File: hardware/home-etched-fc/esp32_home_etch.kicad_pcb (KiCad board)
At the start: 2 copper layers, 100 x 100 mm, 41 parts, among them J1 DevKitC-1 LEFT 1x22, J10 ESC_RR, J11 ESC_RL, J12 OPTIONAL 3V3 UART, J13 F2 MINI: VCC TBD, J14 0-2.5V current input, J2 DevKitC-1 RIGHT 1x22, J3 REGULATED 5V ONLY, J4 MPU6050, J5 BMP280, J6 HMC5883L, J7 SENSE ONLY, J8 ESC_FL, J9 ESC_FR

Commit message: Retain connected ground copper and print three text-free toner masks per A4
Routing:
- added copper zone on B.Cu, net GND

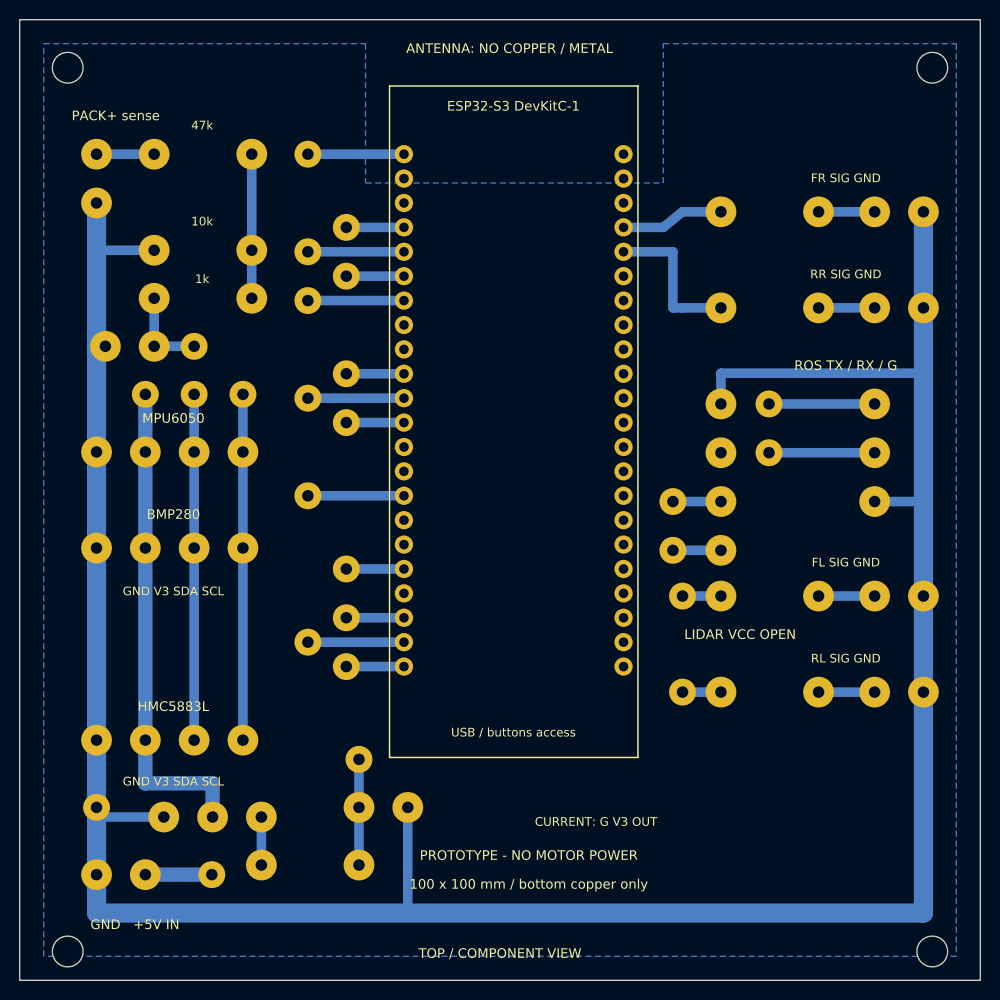
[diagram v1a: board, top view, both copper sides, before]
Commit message: Unify ESP32 firmware, verify optional ROS2 fallback and connect DevKit grounds directly
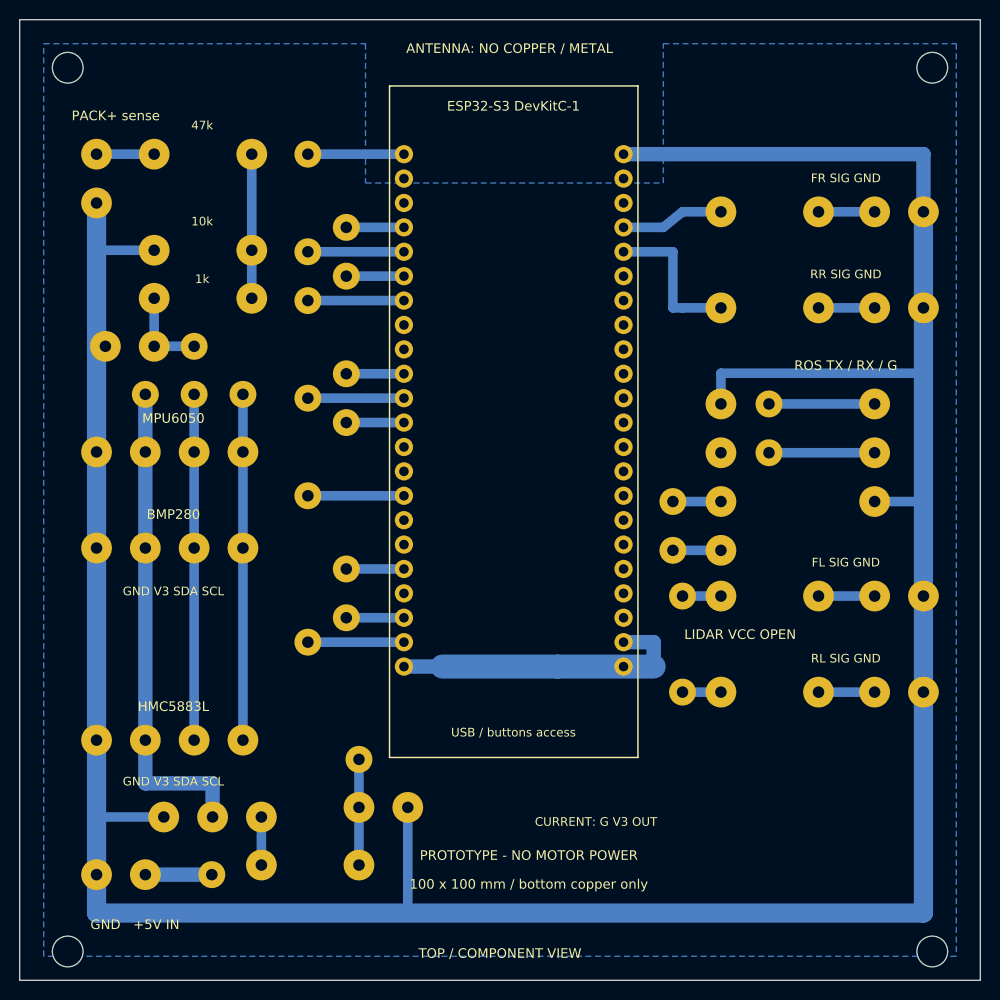
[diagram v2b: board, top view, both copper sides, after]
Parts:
- removed W22: INSULATED_WIRE, HomeEtch:W22
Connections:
- J1 pad 22: GND_MCU -> GND
- J2 pad 1: unconnected-(J2-Pad1) -> GND
- J2 pad 21: unconnected-(J2-Pad21) -> GND
- J2 pad 22: unconnected-(J2-Pad22) -> GND
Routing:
- net GND: track 287.3 -> 359.3 mm
- net GND_MCU: track 6.00 -> 0.00 mm

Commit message: Use solid common-ground pads and verify PCB power rails and toner mask
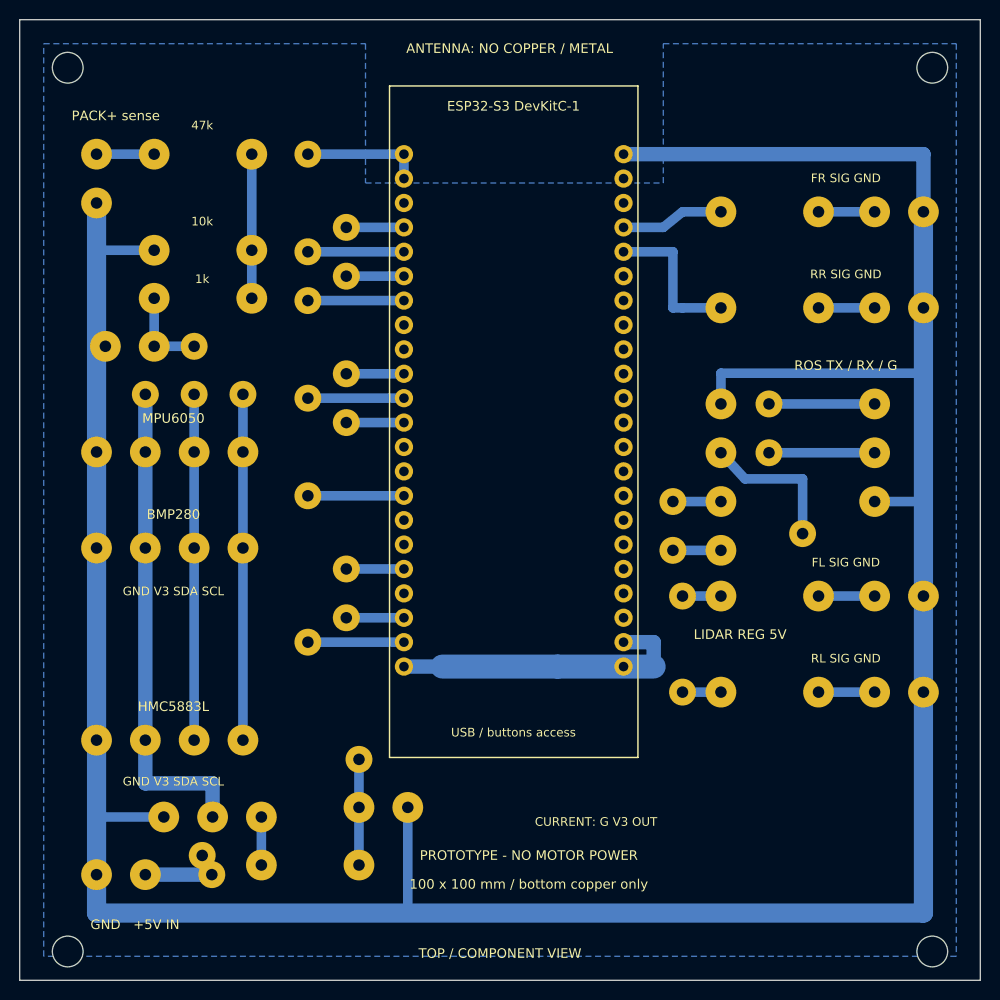
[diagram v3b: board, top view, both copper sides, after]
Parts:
- added W23: INSULATED_WIRE, HomeEtch:W23, F.Cu at (19.0, 87.0)
- J13: value F2 MINI: VCC TBD -> F2 MINI: REG 5V
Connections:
- J1 pad 2: unconnected-(J1-Pad2) -> 3V3
- J13 pad 2: unconnected-(J13-Pad2) -> LIDAR_5V
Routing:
- net LIDAR_5V: track 0.00 -> 15.4 mm
- net 3V3: track 10.0 -> 12.5 mm
- net 5V_EXT: track 6.92 -> 9.16 mm
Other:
- board text added: "LIDAR REG 5V"
- board text removed: "LIDAR VCC OPEN"

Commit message: Verify PCB reference dimensions and regenerate three actual-size copper masks
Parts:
- C1, C2: value 100nF -> 100nF X7R 5mm
- J4: value MPU6050 -> MPU6050 WIRE PORT
- J5: value BMP280 -> BMP280 WIRE PORT
- J6: value HMC5883L -> HMC5883L WIRE PORT
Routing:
- net GND: track 359.3 -> 356.4 mm

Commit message: Fix photo-matched sensor headers and verify single-sided PCB mask
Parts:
- added W24: INSULATED_WIRE, HomeEtch:W24, F.Cu at (8.00, 62.0)
- J13: value F2 MINI: REG 5V -> F2 MINI WIRE PADS
- J4: value MPU6050 WIRE PORT -> GY-521 MPU6050
- J5: value BMP280 WIRE PORT -> GY-BM280 I2C
- J6: value HMC5883L WIRE PORT -> GY-271 MAG
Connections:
- J4 pad 1: GND -> SENS_3V3
- J4 pad 2: SENS_3V3 -> GND
- J4 pad 3: I2C_SDA -> I2C_SCL
- J4 pad 4: I2C_SCL -> I2C_SDA
- J5 pad 1: GND -> SENS_3V3
- J5 pad 2: SENS_3V3 -> GND
- J5 pad 3: I2C_SDA -> I2C_SCL
- J5 pad 4: I2C_SCL -> I2C_SDA
- J6 pad 1: GND -> SENS_3V3
- J6 pad 2: SENS_3V3 -> GND
- J6 pad 3: I2C_SDA -> I2C_SCL
- J6 pad 4: I2C_SCL -> I2C_SDA
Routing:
- net GND: track 356.4 -> 424.7 mm
- net BARO_CSB: track 0.00 -> 7.00 mm
- net SENS_3V3: track 51.0 -> 56.1 mm
- net I2C_SDA: track 36.0 -> 34.0 mm
- net I2C_SCL: track 36.0 -> 37.0 mm
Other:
- board text added: "1:VCC 2:G 3:SCL 4:SDA"
- board text added: "GY-271 MAG"
- board text added: "GY-521 MPU6050"
- board text added: "GY-BM280 I2C"
- board text removed: "BMP280"
- board text removed: "GND V3 SDA SCL"
- board text removed: "HMC5883L"
- board text removed: "MPU6050"
